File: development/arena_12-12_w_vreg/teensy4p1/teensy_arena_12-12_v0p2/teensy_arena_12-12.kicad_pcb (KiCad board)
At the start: 4 copper layers, 228.6 x 228.6 mm, 123 parts, among them J1 Barrel_Jack, J2 Conn_01x04, J3 Conn_01x04, P1 CONN15, P10 CONN15, P11 CONN15, P12 CONN15, P2 CONN15, P3 CONN15, P4 CONN15, P5 CONN15, P6 CONN15, P7 CONN15, P8 CONN15, P9 CONN15, Q2 MOSFET_NCHAN, SW1 SW_SPDT, U1 TXB0108PW, U10 TPS564201DDC, U11 TPS564201DDC, U12 TPS564201DDC, U13 TPS564201DDC, U14 TPS564201DDC, U15 TPS564201DDC, U16 TPS564201DDC, U17 TPS564201DDC, U18 Teensy4.1, U2 TXB0108PW, U3 TXB0108PW, U4 TXB0108PW, U5 TXB0108PW, U6 TPS564201DDC, U7 TPS564201DDC, U8 TPS564201DDC, U9 TPS564201DDC

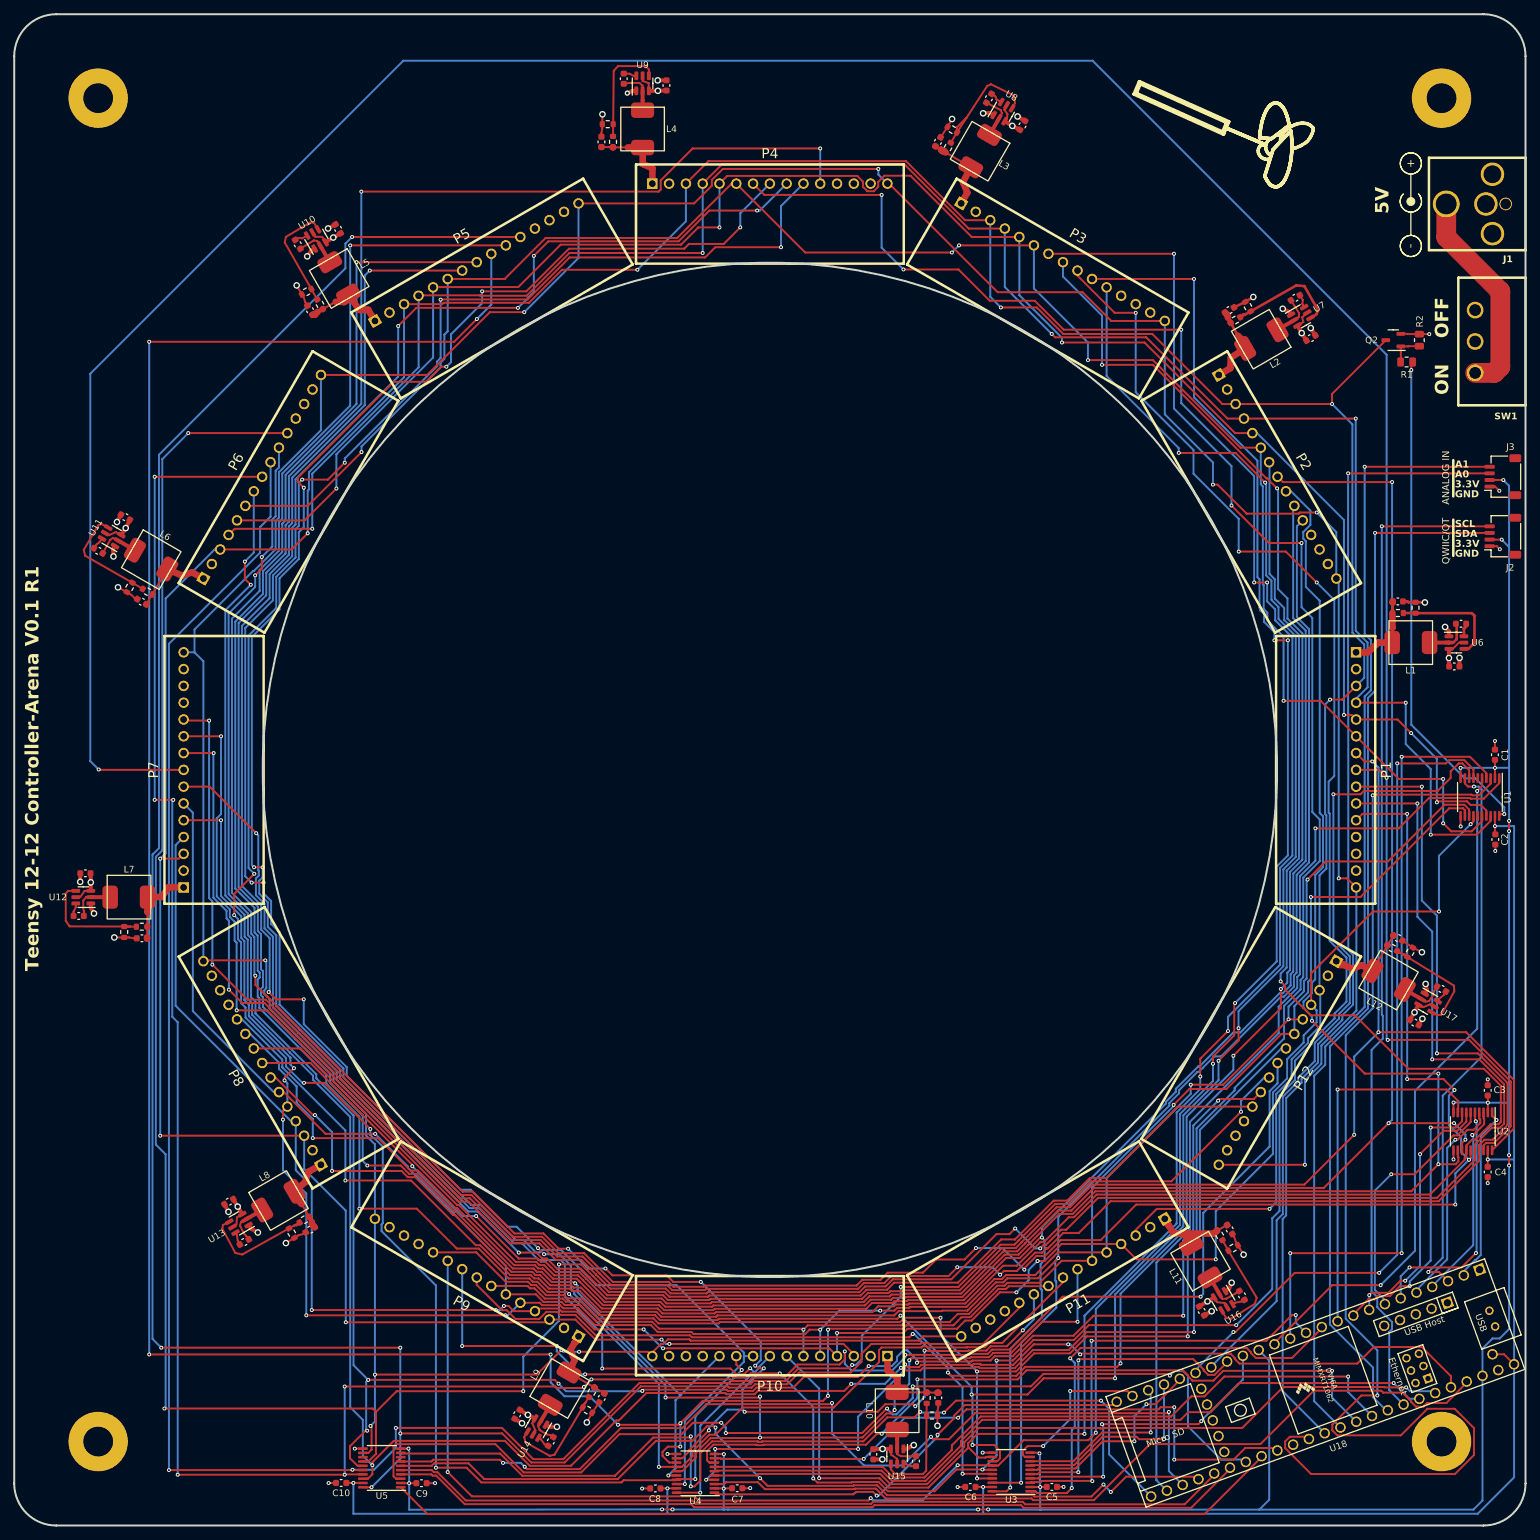
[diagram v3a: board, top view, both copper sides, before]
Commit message: Worked on 6-layer routes.
Worked on adding gnd stiching vias for 12-12 NI arena with vreg. Work on
6-layer route for 12-12 teensy arena with vreg.
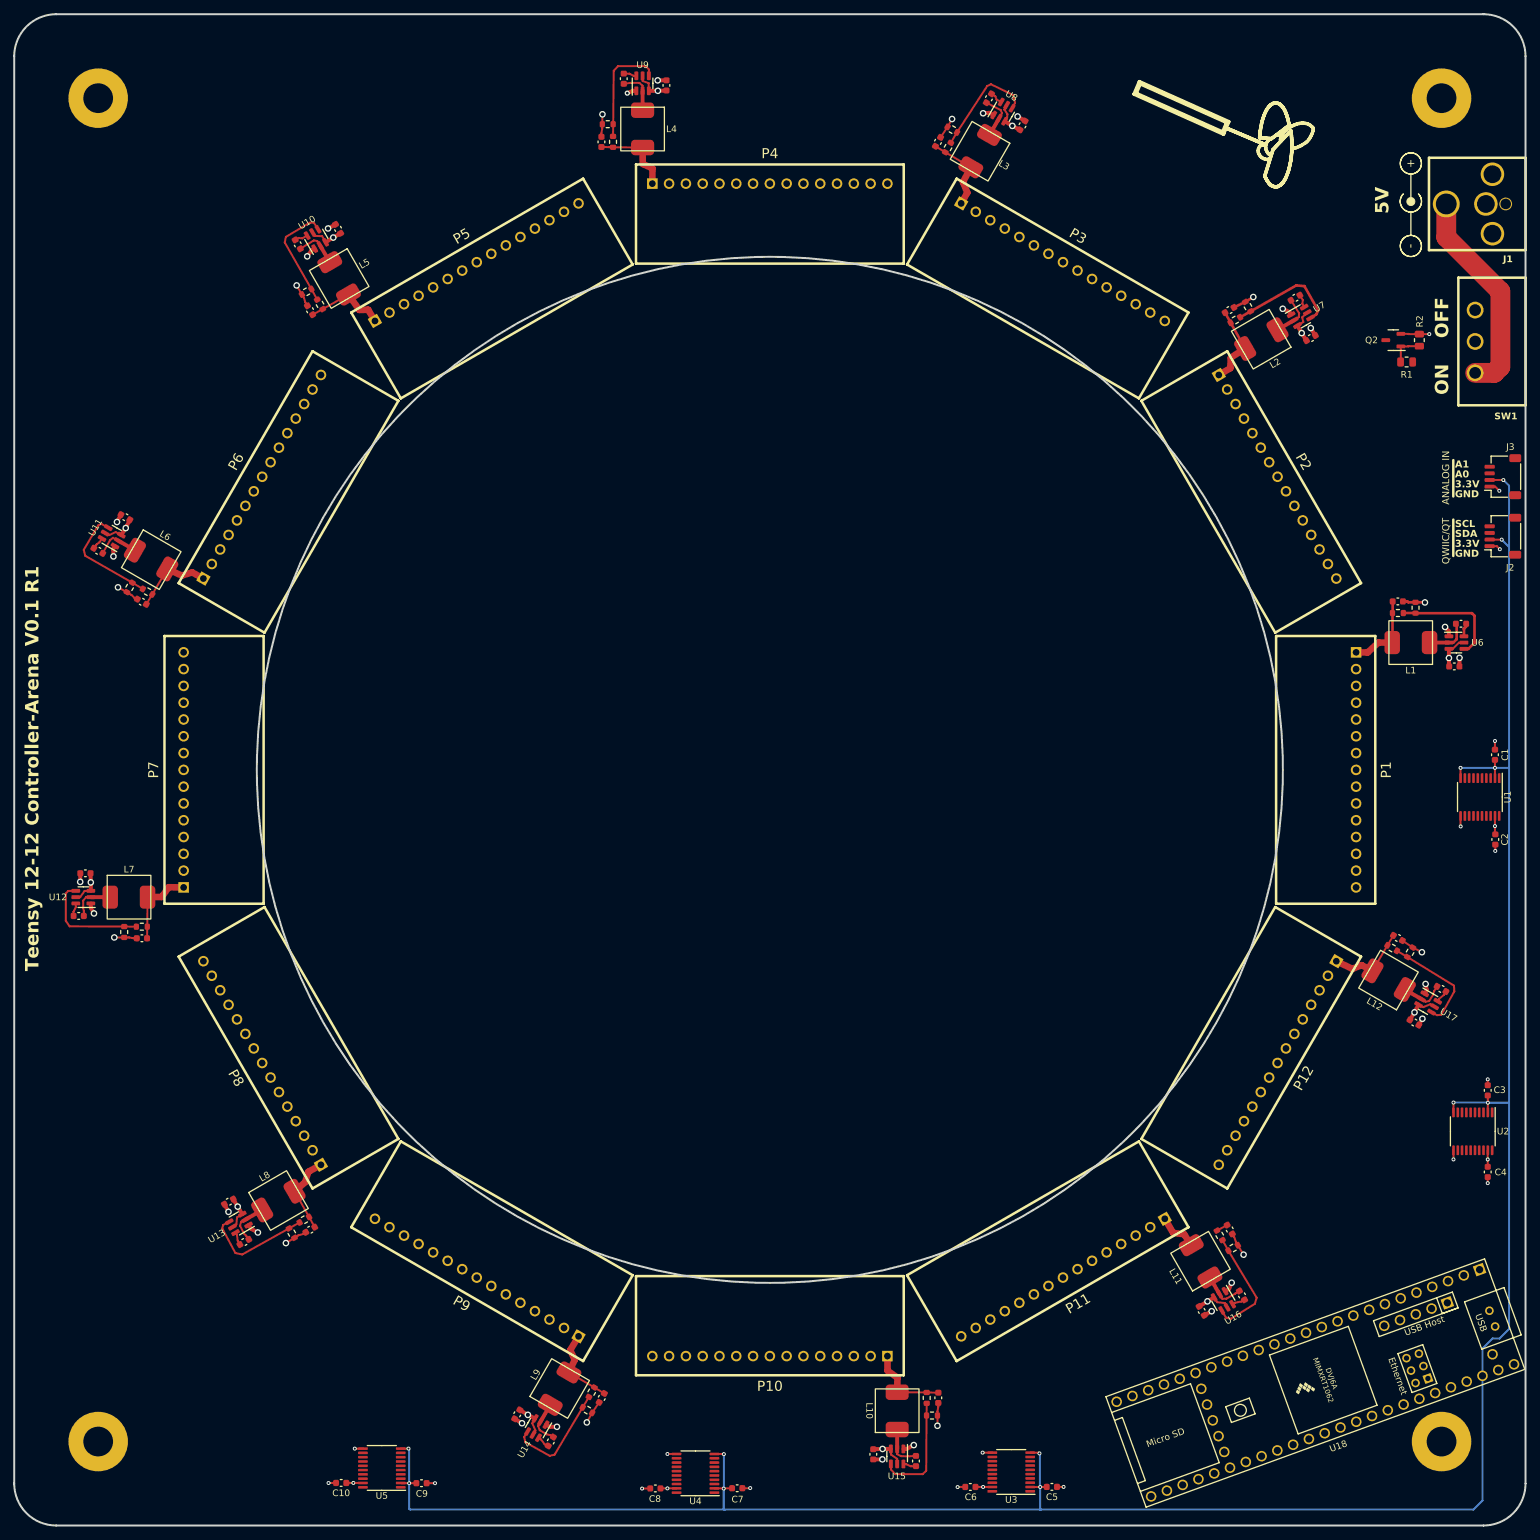
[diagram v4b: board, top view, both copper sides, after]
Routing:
- net /Panel Headers/RESET: track 624.9 -> 0.00 mm, vias 11 -> 0
- net /Level Shifters/PAN5V.EXT_INT: track 603.1 -> 0.00 mm, vias 11 -> 0
- net /Level Shifters/PAN5V.CS_01: track 450.2 -> 0.00 mm, vias 3 -> 0
- net /Level Shifters/PAN5V.CS_26: track 391.9 -> 0.00 mm, vias 11 -> 0
- net /Level Shifters/PAN5V.CS_22: track 382.1 -> 0.00 mm, vias 9 -> 0
- net /Level Shifters/PAN5V.CS_24: track 373.8 -> 0.00 mm, vias 5 -> 0
- net /Level Shifters/PAN5V.CS_29: track 370.1 -> 0.00 mm, vias 4 -> 0
- net /Level Shifters/PAN5V.CS_27: track 361.2 -> 0.00 mm, vias 6 -> 0
- net /Level Shifters/PAN5V.CS_12: track 355.6 -> 0.00 mm, vias 11 -> 0
- net /Level Shifters/PAN5V.CS_25: track 347.8 -> 0.00 mm, vias 6 -> 0
- net /Level Shifters/PAN5V.CS_13: track 345.4 -> 0.00 mm, vias 9 -> 0
- net /Level Shifters/PAN5V.CS_05: track 344.7 -> 0.00 mm, vias 3 -> 0
- net /Level Shifters/PAN5V.CS_28: track 341.4 -> 0.00 mm, vias 10 -> 0
- net /Level Shifters/PAN5V.CS_03: track 339.9 -> 0.00 mm, vias 6 -> 0
- net /Level Shifters/PAN5V.CS_10: track 336.7 -> 0.00 mm, vias 7 -> 0
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- added copper zone on In3.Cu, net +5V
- added copper zone on In4.Cu, net GND
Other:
- outline, holes or cut-outs redrawn
- copper layers 4 -> 6
